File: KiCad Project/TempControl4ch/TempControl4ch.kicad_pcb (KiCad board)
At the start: 2 copper layers, 80 x 60 mm, 44 parts, among them J1 Conn_01x08_Socket, U1 MAX31856, U2 MAX31856, U3 MAX31856, U4 MAX31856, U5 BluePill_Part_Like_SWD_Breako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

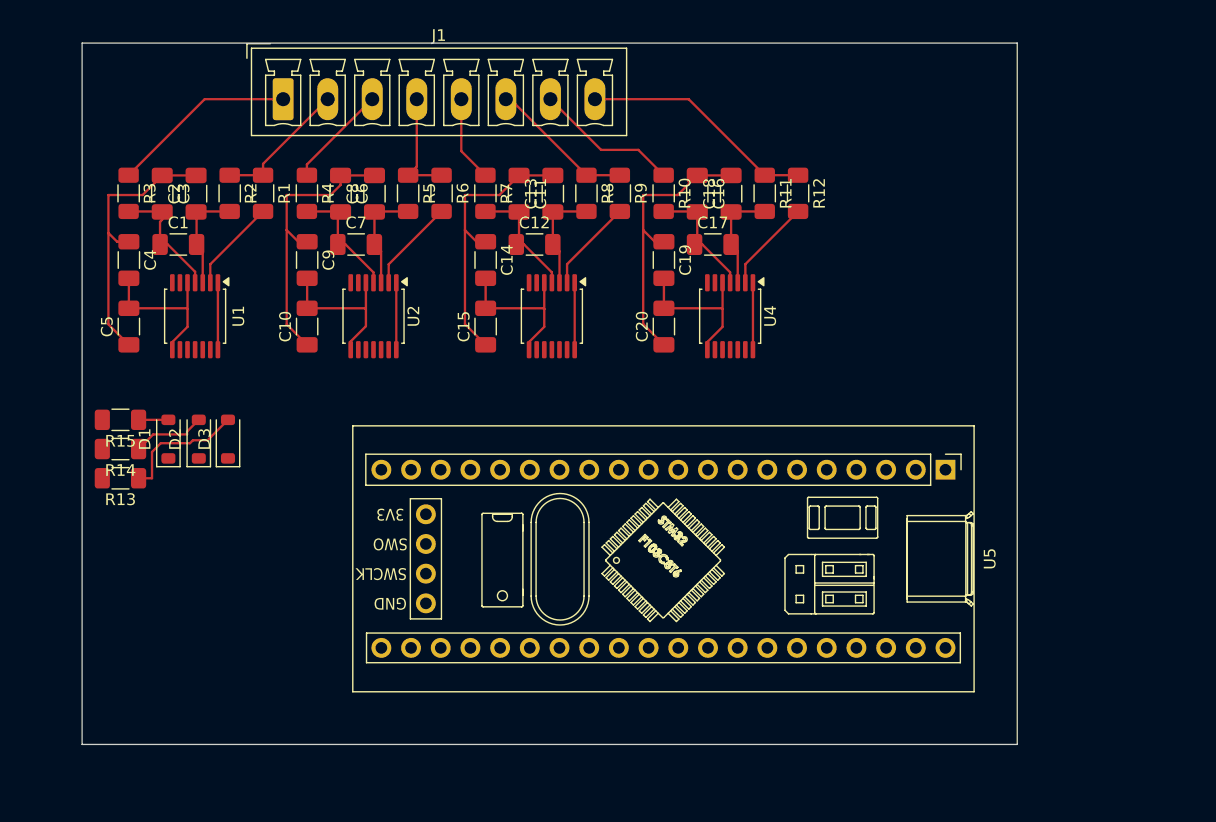
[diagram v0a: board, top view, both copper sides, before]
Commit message: added SPI connections and update schematic & pcb
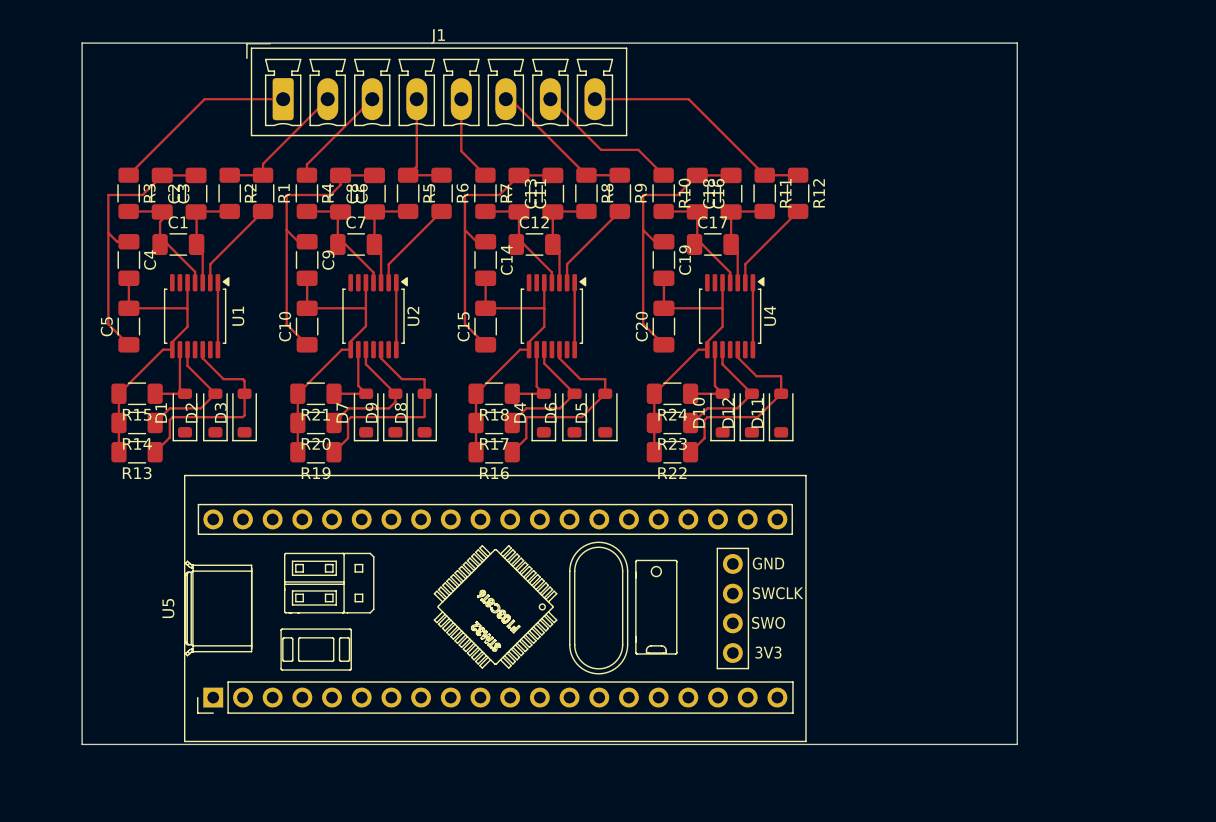
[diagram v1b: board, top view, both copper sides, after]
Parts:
- added D10: 1N4148W, Diode_SMD:D_SOD-123, F.Cu at (172.8, 89.7)
- added D11: 1N4148W, Diode_SMD:D_SOD-123, F.Cu at (177.8, 89.7)
- added D12: 1N4148W, Diode_SMD:D_SOD-123, F.Cu at (175.3, 89.7)
- added D4: 1N4148W, Diode_SMD:D_SOD-123, F.Cu at (157.5, 89.7)
- added D5: 1N4148W, Diode_SMD:D_SOD-123, F.Cu at (162.8, 89.7)
- added D6: 1N4148W, Diode_SMD:D_SOD-123, F.Cu at (160.1, 89.7)
- added D7: 1N4148W, Diode_SMD:D_SOD-123, F.Cu at (142.3, 89.7)
- added D8: 1N4148W, Diode_SMD:D_SOD-123, F.Cu at (147.3, 89.7)
- added D9: 1N4148W, Diode_SMD:D_SOD-123, F.Cu at (144.8, 89.7)
- added R16: 10k, Resistor_SMD:R_1206_3216Metric_Pad1.30x1.75mm_HandSolder, F.Cu at (153.2, 93.0)
- added R17: 10k, Resistor_SMD:R_1206_3216Metric_Pad1.30x1.75mm_HandSolder, F.Cu at (153.2, 90.5)
- added R18: 10k, Resistor_SMD:R_1206_3216Metric_Pad1.30x1.75mm_HandSolder, F.Cu at (153.2, 88.0)
- added R19: 10k, Resistor_SMD:R_1206_3216Metric_Pad1.30x1.75mm_HandSolder, F.Cu at (138.0, 93.0)
- added R20: 10k, Resistor_SMD:R_1206_3216Metric_Pad1.30x1.75mm_HandSolder, F.Cu at (138.0, 90.5)
- added R21: 10k, Resistor_SMD:R_1206_3216Metric_Pad1.30x1.75mm_HandSolder, F.Cu at (138.0, 88.0)
- added R22: 10k, Resistor_SMD:R_1206_3216Metric_Pad1.30x1.75mm_HandSolder, F.Cu at (168.5, 93.0)
- added R23: 10k, Resistor_SMD:R_1206_3216Metric_Pad1.30x1.75mm_HandSolder, F.Cu at (168.5, 90.5)
- added R24: 10k, Resistor_SMD:R_1206_3216Metric_Pad1.30x1.75mm_HandSolder, F.Cu at (168.5, 88.0)
- R13, R14, R15: value 2k -> 10k
- moved U5 65.6 mm to (129.2, 114.0), turned to 90 degrees
- moved R13 2.64 mm to (122.7, 93.0)
- moved R14 2.64 mm to (122.7, 90.5)
- moved R15 2.64 mm to (122.7, 88.0)
- moved D3 2.64 mm to (131.9, 89.7)
- moved D1 2.64 mm to (126.8, 89.7)
- moved D2 2.64 mm to (129.4, 89.7)
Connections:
- D1 pad 1: unconnected-(D1-K-Pad1) -> Net-(D1-K)
- D2 pad 1: unconnected-(D2-K-Pad1) -> Net-(D12-K)
- D3 pad 1: unconnected-(D3-K-Pad1) -> Net-(D11-K)
- U1 pad 11: unconnected-(U1-SDO-Pad11) -> Net-(U1-SDO)
- U2 pad 10: unconnected-(U2-SCK-Pad10) -> Net-(D9-A)
- U2 pad 11: unconnected-(U2-SDO-Pad11) -> Net-(U1-SDO)
- U2 pad 12: unconnected-(U2-SDI-Pad12) -> Net-(D8-A)
- U2 pad 9: unconnected-(U2-~{CS}-Pad9) -> Net-(D7-A)
- U3 pad 10: unconnected-(U3-SCK-Pad10) -> Net-(D6-A)
- U3 pad 11: unconnected-(U3-SDO-Pad11) -> Net-(U1-SDO)
- U3 pad 12: unconnected-(U3-SDI-Pad12) -> Net-(D5-A)
- U3 pad 9: unconnected-(U3-~{CS}-Pad9) -> Net-(D4-A)
- U4 pad 10: unconnected-(U4-SCK-Pad10) -> Net-(D12-A)
- U4 pad 11: unconnected-(U4-SDO-Pad11) -> Net-(U1-SDO)
- U4 pad 12: unconnected-(U4-SDI-Pad12) -> Net-(D11-A)
- U4 pad 9: unconnected-(U4-~{CS}-Pad9) -> Net-(D10-A)
- U5 pad 26: unconnected-(U5-PA1-Pad26) -> Net-(D10-K)
- U5 pad 27: unconnected-(U5-PA2-Pad27) -> Net-(D4-K)
- U5 pad 28: unconnected-(U5-PA3-Pad28) -> Net-(D7-K)
- U5 pad 29: unconnected-(U5-PA4-Pad29) -> Net-(D1-K)
- U5 pad 30: unconnected-(U5-PA5-Pad30) -> Net-(D12-K)
- U5 pad 31: unconnected-(U5-PA6-Pad31) -> Net-(U1-SDO)
- U5 pad 32: unconnected-(U5-PA7-Pad32) -> Net-(D11-K)
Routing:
- net VDD: track 55.5 -> 99.9 mm
- net Net-(D8-A): track 0.00 -> 18.3 mm
- net Net-(D5-A): track 0.00 -> 17.7 mm
- net Net-(D11-A): track 0.00 -> 17.2 mm
- net Net-(D9-A): track 0.00 -> 11.5 mm
- net Net-(D6-A): track 0.00 -> 11.2 mm
- net Net-(D12-A): track 0.00 -> 11.1 mm
- net Net-(D3-A): track 11.0 -> 17.9 mm
- net Net-(D7-A): track 0.00 -> 6.80 mm
- net Net-(D10-A): track 0.00 -> 6.79 mm
- net Net-(D4-A): track 0.00 -> 6.72 mm
- net Net-(D2-A): track 6.33 -> 10.9 mm
- net Net-(D1-A): track 2.55 -> 6.50 mm

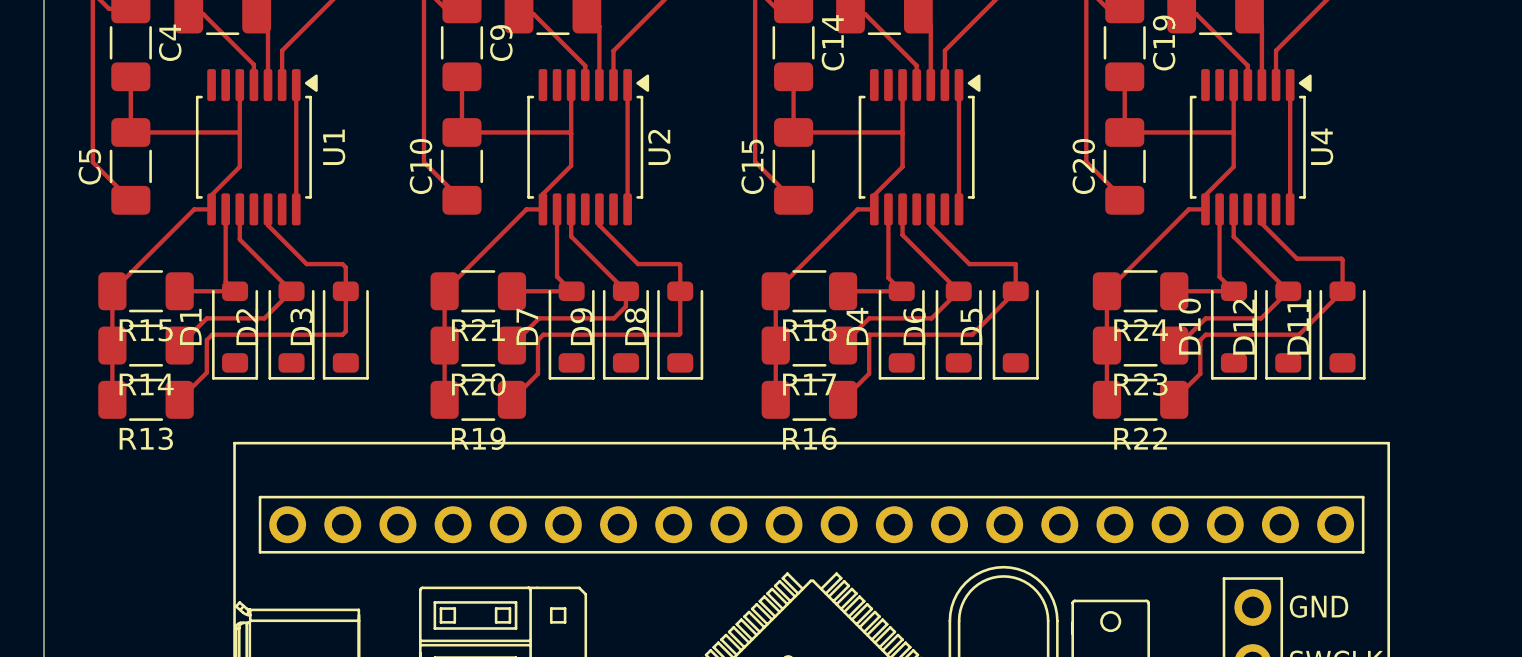
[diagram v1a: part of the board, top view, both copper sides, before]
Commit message: update schematic & pcb, all pcb wiring is completed
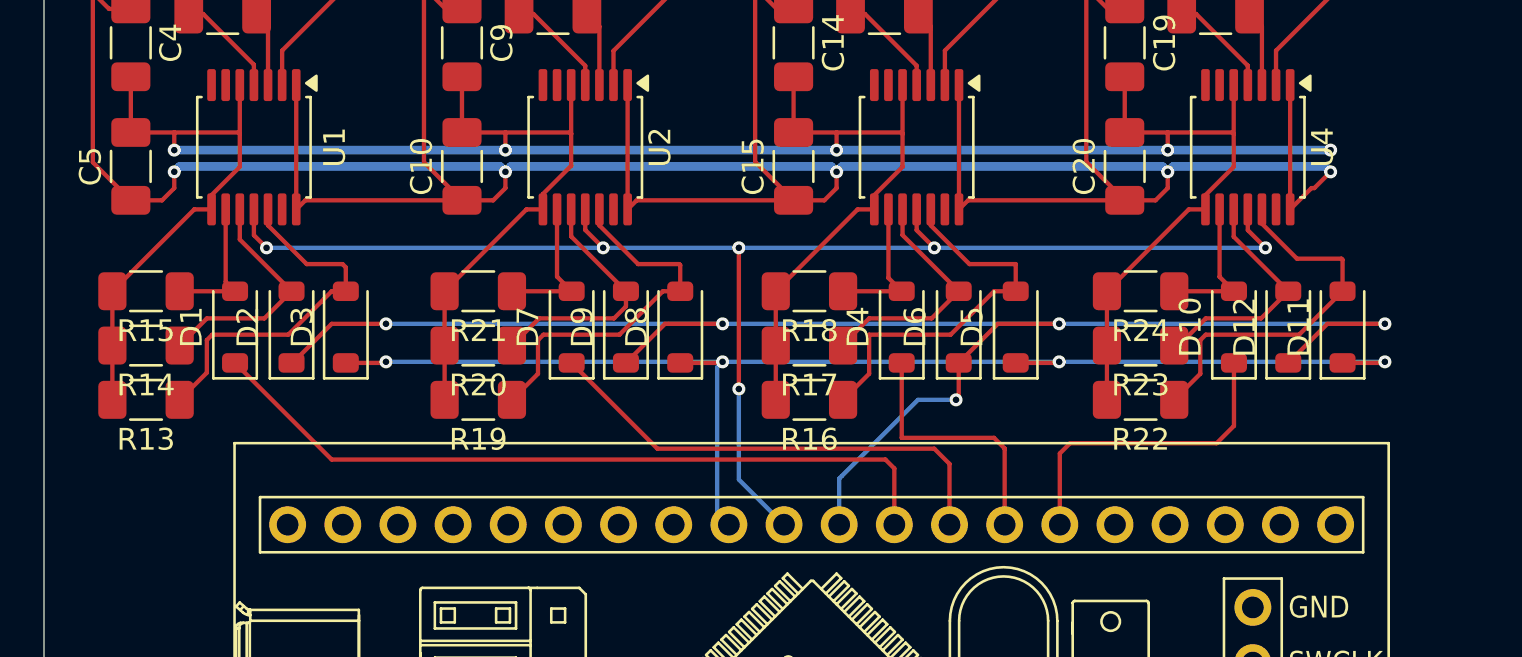
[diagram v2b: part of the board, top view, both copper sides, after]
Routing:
- net GNDREF: track 119.0 -> 210.9 mm, vias 0 -> 5
- net Net-(D12-K): track 0.00 -> 77.6 mm, vias 0 -> 5
- net Net-(U1-SDO): track 0.00 -> 67.9 mm, vias 0 -> 6
- net Net-(D11-K): track 0.00 -> 61.7 mm, vias 0 -> 4
- net VDD: track 99.9 -> 156.4 mm, vias 0 -> 5
- net Net-(D1-K): track 0.00 -> 35.0 mm
- net Net-(D7-K): track 0.00 -> 22.1 mm
- net Net-(D10-K): track 0.00 -> 14.7 mm
- net Net-(D4-K): track 0.00 -> 11.9 mm
- net Net-(D8-A): track 18.3 -> 17.1 mm
- net Net-(D3-A): track 17.9 -> 16.8 mm

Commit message: added 24v to 5v converter schematic
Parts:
- added C21: 10uF, Capacitor_SMD:C_1206_3216Metric_Pad1.33x1.80mm_HandSolder, F.Cu at (190.5, 82.0)
- added C22: 0.1uF, Capacitor_SMD:C_1206_3216Metric_Pad1.33x1.80mm_HandSolder, F.Cu at (193.2, 82.0)
- added C23: 0.1uF, Capacitor_SMD:C_1206_3216Metric_Pad1.33x1.80mm_HandSolder, F.Cu at (198.8, 78.0)
- added C24: 22uF, Capacitor_SMD:C_1206_3216Metric_Pad1.33x1.80mm_HandSolder, F.Cu at (188.2, 72.7)
- added C25: 22uF, Capacitor_SMD:C_1206_3216Metric_Pad1.33x1.80mm_HandSolder, F.Cu at (188.2, 76.0)
- added C26: 75pF, Capacitor_SMD:C_1206_3216Metric_Pad1.33x1.80mm_HandSolder, F.Cu at (197.8, 92.8)
- added J2: Conn_01x02_Socket, Connector_Phoenix_MC:PhoenixContact_MCV_1,5_2-G-3.5_1x02_P3.50mm_Vertical, F.Cu at (189.5, 61.6)
- added L1: 15uH, Inductor_SMD:L_Sumida_CDMC6D28_7.25x6.5mm, F.Cu at (185.2, 82.0)
- added R25: 511k, Resistor_SMD:R_1206_3216Metric_Pad1.30x1.75mm_HandSolder, F.Cu at (198.2, 85.8)
- added R26: 105k, Resistor_SMD:R_1206_3216Metric_Pad1.30x1.75mm_HandSolder, F.Cu at (203.0, 82.0)
- added R27: 49.9, Resistor_SMD:R_1206_3216Metric_Pad1.30x1.75mm_HandSolder, F.Cu at (192.0, 89.2)
- added R28: 100k, Resistor_SMD:R_1206_3216Metric_Pad1.30x1.75mm_HandSolder, F.Cu at (197.8, 89.2)
- added R29: 13.3k, Resistor_SMD:R_1206_3216Metric_Pad1.30x1.75mm_HandSolder, F.Cu at (205.8, 82.0)
- added U6: TPS54202DDC, Package_TO_SOT_SMD:SOT-23-6, F.Cu at (198.2, 82.0)
- moved U5 6.47 mm to (122.8, 114.0)
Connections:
- U5 pad 18: unconnected-(U5-5V-Pad18) -> +5V
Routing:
- net Net-(D7-K): track 22.1 -> 15.3 mm
- net Net-(D10-K): track 14.7 -> 21.5 mm
- net Net-(D1-K): track 35.0 -> 28.5 mm
- net Net-(D12-K): track 77.6 -> 82.8 mm
- net Net-(D4-K): track 11.9 -> 8.17 mm
- net Net-(D11-K): track 61.7 -> 63.9 mm
- net Net-(U1-SDO): track 67.9 -> 68.9 mm
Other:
- board size 80 x 60 mm -> 100 x 60 mm

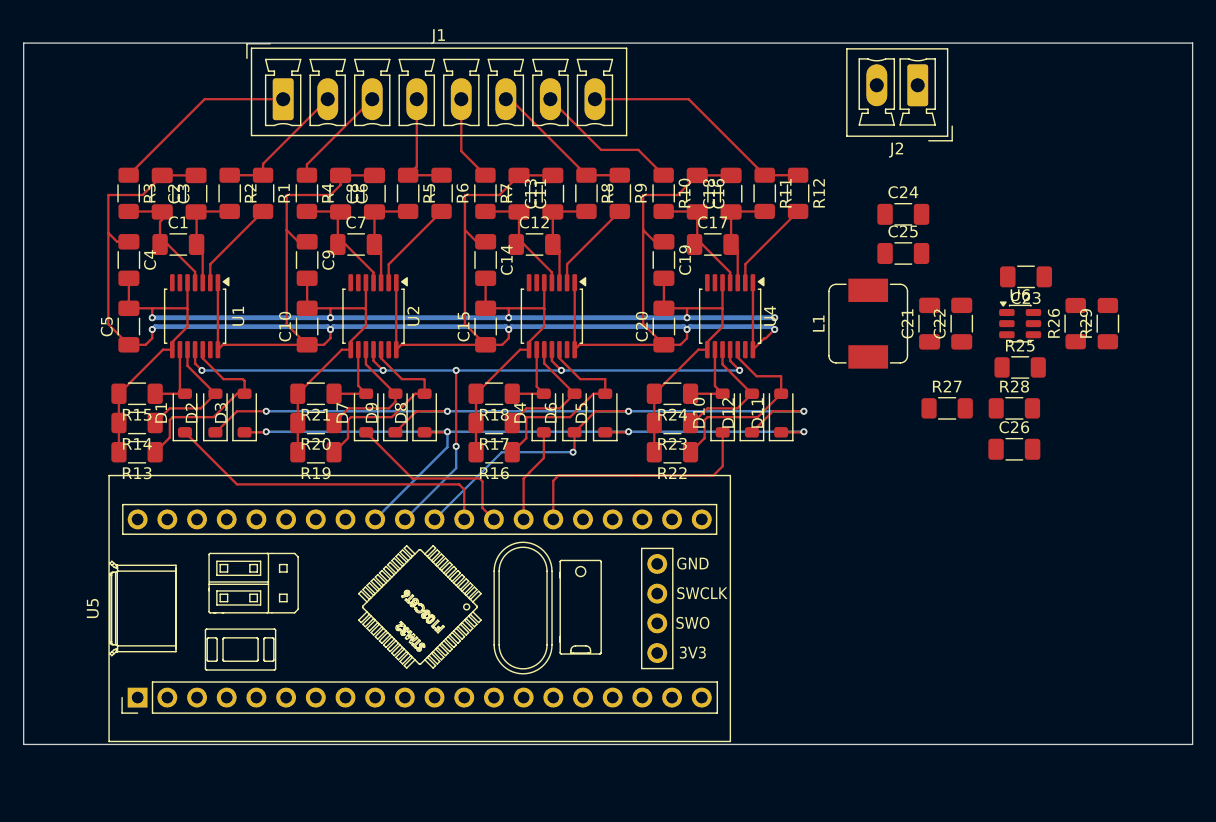
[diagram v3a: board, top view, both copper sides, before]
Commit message: update supply circuit pcb design
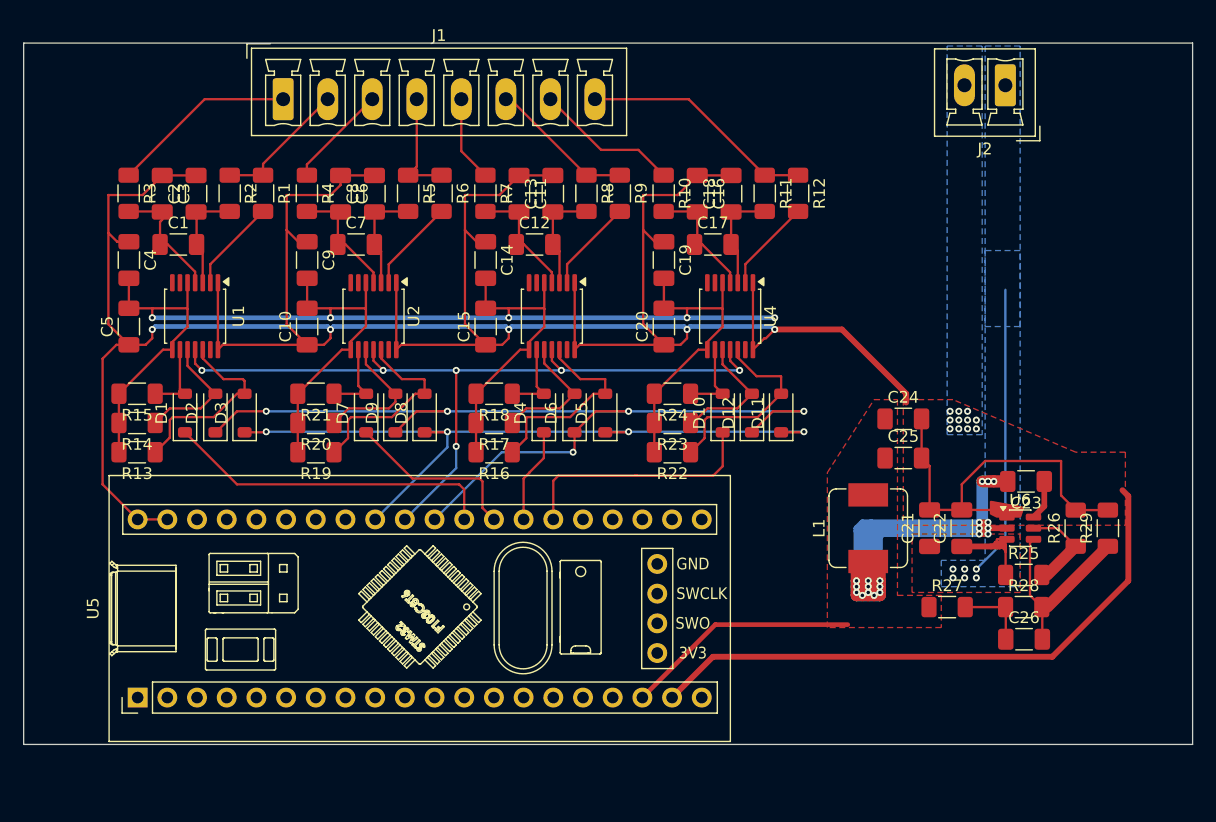
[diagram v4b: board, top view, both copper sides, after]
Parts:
- moved R25 17.8 mm to (198.6, 103.5)
- moved C21 17.5 mm to (190.5, 99.5)
- moved C22 17.5 mm to (193.2, 99.5)
- moved C23 17.5 mm to (198.8, 95.5)
- moved C24 17.5 mm to (188.2, 90.2)
- moved C25 17.5 mm to (188.2, 93.5)
- moved L1 17.5 mm to (185.2, 99.5)
- moved R26 17.5 mm to (203.0, 99.5)
- moved R29 17.5 mm to (205.8, 99.5)
- moved U6 17.5 mm to (198.2, 99.5)
- moved R28 17.0 mm to (198.6, 106.2)
- moved R27 17.0 mm to (192.0, 106.2)
- moved C26 16.3 mm to (198.6, 109.0)
- moved J2 7.50 mm to (197.0, 61.6)
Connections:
- U5 pad 19: unconnected-(U5-GND-Pad19) -> GNDREF
- U5 pad 39: unconnected-(U5-GND-Pad39) -> GNDREF
- U5 pad 40: unconnected-(U5-GND-Pad40) -> GNDREF
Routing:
- net GNDREF: track 210.9 -> 331.8 mm, vias 5 -> 16
- net Net-(U6-SW): track 0.00 -> 104.4 mm, vias 0 -> 21
- net /+24v: track 0.00 -> 37.4 mm, vias 0 -> 6
- net +5V: track 0.00 -> 20.2 mm
- net Net-(U6-FB): track 0.00 -> 16.9 mm
- net Net-(U6-EN): track 0.00 -> 8.17 mm
- net Net-(C26-Pad1): track 0.00 -> 6.21 mm
- net Net-(U6-BOOT): track 0.00 -> 3.43 mm
- added copper zone on F.Cu, net +5V
- added copper zone on B.Cu, net /+24v
- added copper zone on F.Cu, net /+24v
- added copper zone on B.Cu, net GNDREF
- added copper zone on F.Cu, net GNDREF
